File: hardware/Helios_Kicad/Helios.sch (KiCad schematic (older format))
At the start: 23 parts, among them P1 USB_B, P2 CONN_01X25-SHIELD, U1 IP4220CZ6

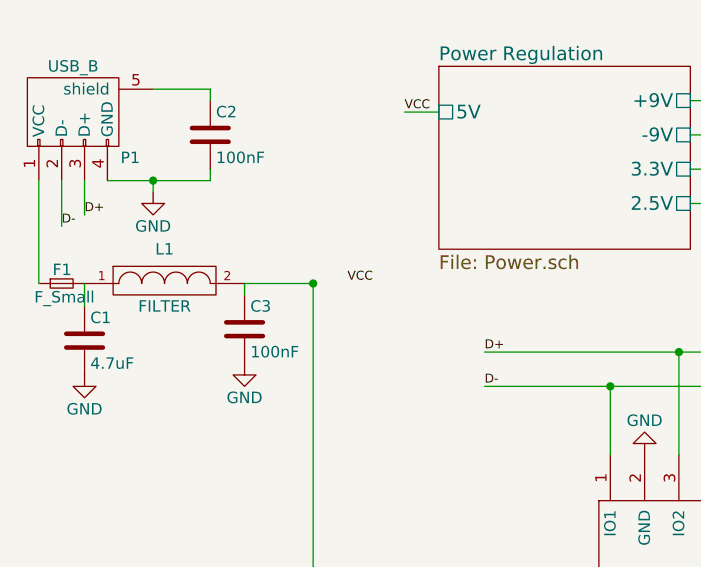
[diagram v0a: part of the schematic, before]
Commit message: driver finished but untested
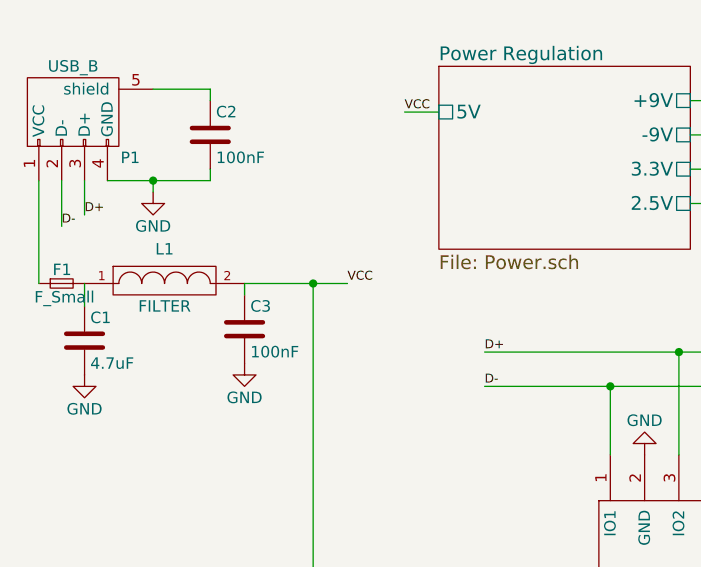
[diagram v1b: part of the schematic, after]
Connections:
- net VCC: now also C3.1, L1.2, U1.5 (Vp)
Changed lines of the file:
@@
 $EndSheet
 $Comp
-L GND #PWR01
+L GND #PWR6
 U 1 1 56B34131
 P 10750 4000
-F 0 "#PWR01" H 10750 3750 50  0001 C CNN
+F 0 "#PWR6" H 10750 3750 50  0001 C CNN
 F 1 "GND" H 10750 3850 50  0000 C CNN
 F 2 "" H 10750 4000 50  0000 C CNN
@@
 $EndComp
 $Comp
-L GND #PWR02
+L GND #PWR5
 U 1 1 56C4FEF7
 P 10700 2400
-F 0 "#PWR02" H 10700 2150 50  0001 C CNN
+F 0 "#PWR5" H 10700 2150 50  0001 C CNN
 F 1 "GND" H 10700 2250 50  0000 C CNN
 F 2 "" H 10700 2400 50  0000 C CNN
@@
 D+
 $Comp
-L GND #PWR03
+L GND #PWR2
 U 1 1 56ED04E3
 P 1450 2650
-F 0 "#PWR03" H 1450 2400 50  0001 C CNN
+F 0 "#PWR2" H 1450 2400 50  0001 C CNN
 F 1 "GND" H 1450 2500 50  0000 C CNN
 F 2 "" H 1450 2650 50  0000 C CNN
@@
 $EndComp
 $Comp
-L GND #PWR04
+L GND #PWR3
 U 1 1 5739A27B
 P 1850 3400
-F 0 "#PWR04" H 1850 3150 50  0001 C CNN
+F 0 "#PWR3" H 1850 3150 50  0001 C CNN
 F 1 "GND" H 1850 3250 50  0000 C CNN
 F 2 "" H 1850 3400 50  0000 C CNN
@@
 $EndComp
 $Comp
-L GND #PWR05
+L GND #PWR4
 U 1 1 575A19B8
 P 3600 3800
-F 0 "#PWR05" H 3600 3550 50  0001 C CNN
+F 0 "#PWR4" H 3600 3550 50  0001 C CNN
 F 1 "GND" H 3600 3650 50  0000 C CNN
 F 2 "" H 3600 3800 50  0000 C CNN
@@
 $EndComp
 $Comp
-L GND #PWR06
+L GND #PWR1
 U 1 1 575963D0
 P 1150 3450
-F 0 "#PWR06" H 1150 3200 50  0001 C CNN
+F 0 "#PWR1" H 1150 3200 50  0001 C CNN
 F 1 "GND" H 1150 3300 50  0000 C CNN
 F 2 "" H 1150 3450 50  0000 C CNN
@@
 $EndComp
 Wire Wire Line
-	1850 3050 2150 3050
+	1850 3050 2300 3050
 Wire Wire Line
 	1150 3050 1150 3150

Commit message: redone pcb, driver and firmware working-ish
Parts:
- removed R10, R12, R14, R8: 150, Resistors_SMD:R_0603, symbol R
- C1: footprint Capacitors_SMD:C_0805 -> Capacitors_SMD:C_0603
- renumbered R13 to R10, R15 to R11, R9 to R8, R11 to R9
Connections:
- net GND: now also P2.16 (P16), P2.18 (P18), P2.19 (P19), P2.20 (P20)
- net Microcontroller/ERASE: no longer names the net of U1.6 (IO4)
- no-connect marks 2 -> 3

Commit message: rev 1.1 pcb final
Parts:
- C1: footprint Capacitors_SMD:C_0603 -> Capacitors_SMD:c_elec_4x5.3
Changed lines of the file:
@@
 $EndSheet
 $Comp
-L GND #PWR01
+L GND #PWR6
 U 1 1 56B34131
 P 10750 4000
-F 0 "#PWR01" H 10750 3750 50  0001 C CNN
+F 0 "#PWR6" H 10750 3750 50  0001 C CNN
 F 1 "GND" H 10750 3850 50  0000 C CNN
 F 2 "" H 10750 4000 50  0000 C CNN
@@
 $EndComp
 $Comp
-L GND #PWR02
+L GND #PWR5
 U 1 1 56C4FEF7
 P 10700 2400
-F 0 "#PWR02" H 10700 2150 50  0001 C CNN
+F 0 "#PWR5" H 10700 2150 50  0001 C CNN
 F 1 "GND" H 10700 2250 50  0000 C CNN
 F 2 "" H 10700 2400 50  0000 C CNN
@@
 D+
 $Comp
-L GND #PWR03
+L GND #PWR2
 U 1 1 56ED04E3
 P 1450 2650
-F 0 "#PWR03" H 1450 2400 50  0001 C CNN
+F 0 "#PWR2" H 1450 2400 50  0001 C CNN
 F 1 "GND" H 1450 2500 50  0000 C CNN
 F 2 "" H 1450 2650 50  0000 C CNN
@@
 $EndComp
 $Comp
-L GND #PWR04
+L GND #PWR3
 U 1 1 5739A27B
 P 1850 3400
-F 0 "#PWR04" H 1850 3150 50  0001 C CNN
+F 0 "#PWR3" H 1850 3150 50  0001 C CNN
 F 1 "GND" H 1850 3250 50  0000 C CNN
 F 2 "" H 1850 3400 50  0000 C CNN
@@
 $EndComp
 $Comp
-L GND #PWR05
+L GND #PWR4
 U 1 1 575A19B8
 P 3600 3800
-F 0 "#PWR05" H 3600 3550 50  0001 C CNN
+F 0 "#PWR4" H 3600 3550 50  0001 C CNN
 F 1 "GND" H 3600 3650 50  0000 C CNN
 F 2 "" H 3600 3800 50  0000 C CNN
@@
 F 0 "C1" H 1175 3400 50  0000 L CNN
 F 1 "4.7uF" H 1175 3200 50  0000 L CNN
-F 2 "Capacitors_SMD:C_0603" H 1188 3150 50  0001 C CNN
+F 2 "Capacitors_SMD:c_elec_4x5.3" H 1188 3150 50  0001 C CNN
 F 3 "" H 1150 3300 50  0000 C CNN
 	1    1150 3300
@@
 $EndComp
 $Comp
-L GND #PWR06
+L GND #PWR1
 U 1 1 575963D0
 P 1150 3450
-F 0 "#PWR06" H 1150 3200 50  0001 C CNN
+F 0 "#PWR1" H 1150 3200 50  0001 C CNN
 F 1 "GND" H 1150 3300 50  0000 C CNN
 F 2 "" H 1150 3450 50  0000 C CNN
